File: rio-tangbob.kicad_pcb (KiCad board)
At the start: 2 copper layers, 90.3 x 72.8 mm, 70 parts, among them J1 Conn_02x13_Odd_Even, J2 Conn_01x03, J3 Conn_02x13_Odd_Even, J4 Conn_01x03, J5 Conn_01x03, J6 Conn_01x03, U1 Tang_Nano_9k, U2 WIZ850io, U3 TXS0108EPW, U4 TXS0108EPW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

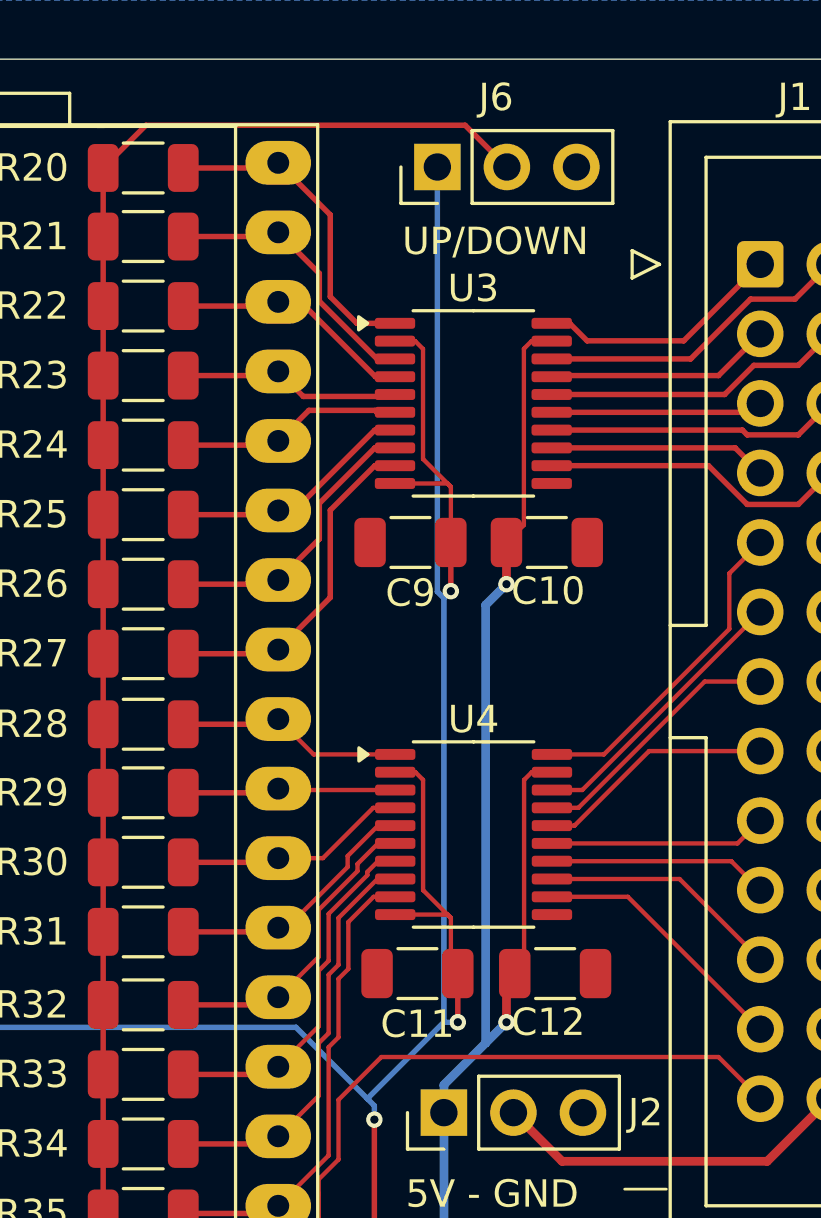
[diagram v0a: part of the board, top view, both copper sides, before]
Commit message: set U3+U4 voltage to ~2.7V
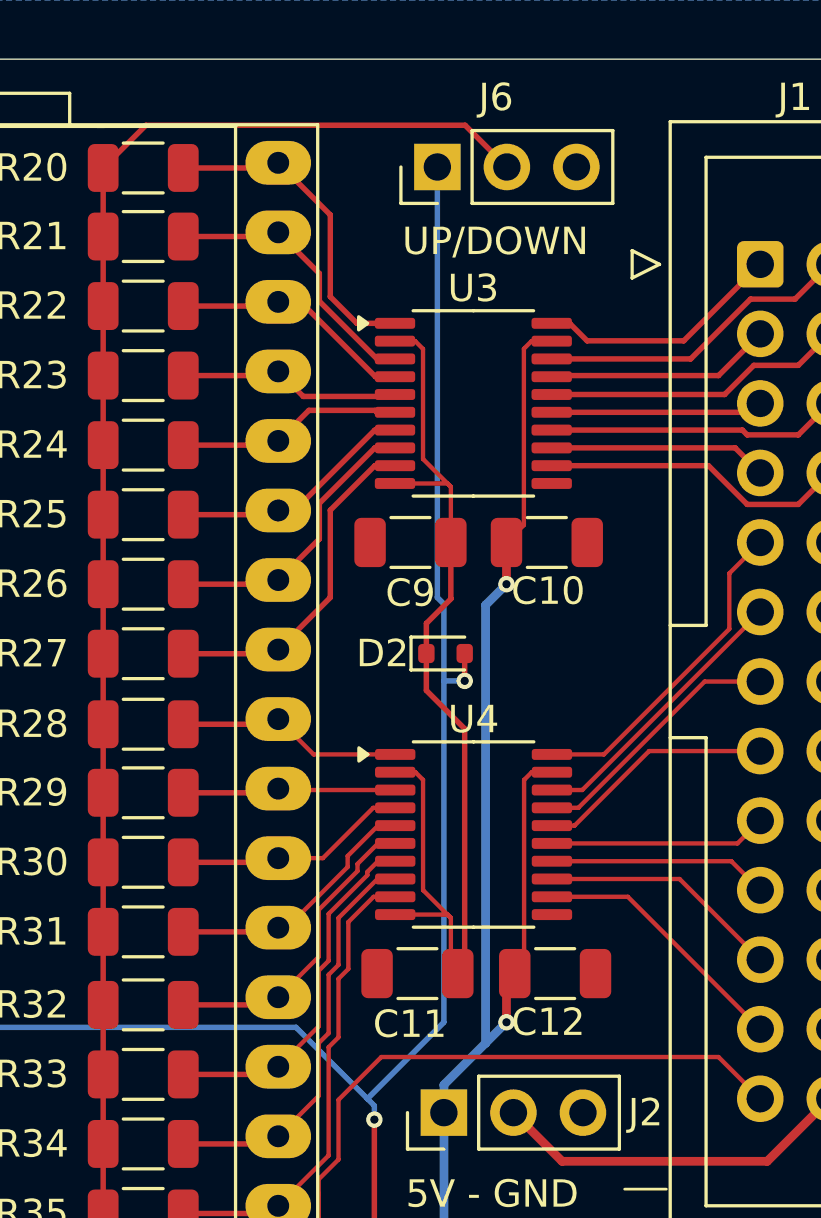
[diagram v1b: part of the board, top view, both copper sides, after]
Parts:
- added D2: 1N4148WT, Diode_SMD:D_SOD-523, F.Cu at (142.3, 64.0)
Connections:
- C11 pad 1: 3V3 -> 2V7
- C9 pad 1: 3V3 -> 2V7
- U3 pad 10: 3V3 -> 2V7
- U3 pad 2: 3V3 -> 2V7
- U4 pad 10: 3V3 -> 2V7
- U4 pad 2: 3V3 -> 2V7
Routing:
- net 2V7: track 0.00 -> 38.3 mm
- net 3V3: track 255.2 -> 231.0 mm, vias 7 -> 6
